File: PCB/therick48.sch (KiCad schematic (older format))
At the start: 125 parts, among them J1 TYPE-C-31-M12_13, J2 AVR-ISP-6, K1 KEYSW, K10 KEYSW, K11 KEYSW, K12 KEYSW, K13 KEYSW, K14 KEYSW, K15 KEYSW, K16 KEYSW, K17 KEYSW, K18 KEYSW, K19 KEYSW, K2 KEYSW, K20 KEYSW, K21 KEYSW, K22 KEYSW, K23 KEYSW, K24 KEYSW, K25 KEYSW, K26 KEYSW, K27 KEYSW, K28 KEYSW, K29 KEYSW, K3 KEYSW, K30 KEYSW, K31 KEYSW, K32 KEYSW, K33 KEYSW, K34 KEYSW, K35 KEYSW, K36 KEYSW, K37 KEYSW, K38 KEYSW, K39 KEYSW, K4 KEYSW, K40 KEYSW, K41 KEYSW, K42 KEYSW, K43 KEYSW, K44 KEYSW, K45 KEYSW, K46 KEYSW, K47 KEYSW, K48 KEYSW, K5 KEYSW, K6 KEYSW, K7 KEYSW, K8 KEYSW, K9 KEYSW, SW1 SW_PUSH, U1 ATMEGA32U4, U2 HOLE, U3 USBLC6-2SC6, U8 HOLE, Y1 16MHz

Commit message: Add Gerbers
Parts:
- removed U8: HOLE, Artwork:QMKBadgeSmall, symbol lets_split-cache:HOLE
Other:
- note removed: "QMK"
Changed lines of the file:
@@
 EESchema Schematic File Version 4
-LIBS:therick-cache
+LIBS:therick48-cache
 EELAYER 29 0
 EELAYER END
@@
 Wire Notes Line
 	9100 4650 9100 6000
-$Comp
-L lets_split-cache:HOLE U8
-U 1 1 5E36C5AD
-P 10100 4250
-F 0 "U8" H 10278 4303 60  0000 L CNN
-F 1 "HOLE" H 10278 4197 60  0000 L CNN
-F 2 "Artwork:QMKBadgeSmall" H 10100 4250 60  0001 C CNN
-F 3 "" H 10100 4250 60  0001 C CNN
-	1    10100 4250
-	1    0    0    -1
-$EndComp
-Text Notes 10000 4300 0    50   ~ 0
-QMK
 NoConn ~ 6700 5200
 NoConn ~ 6700 5300

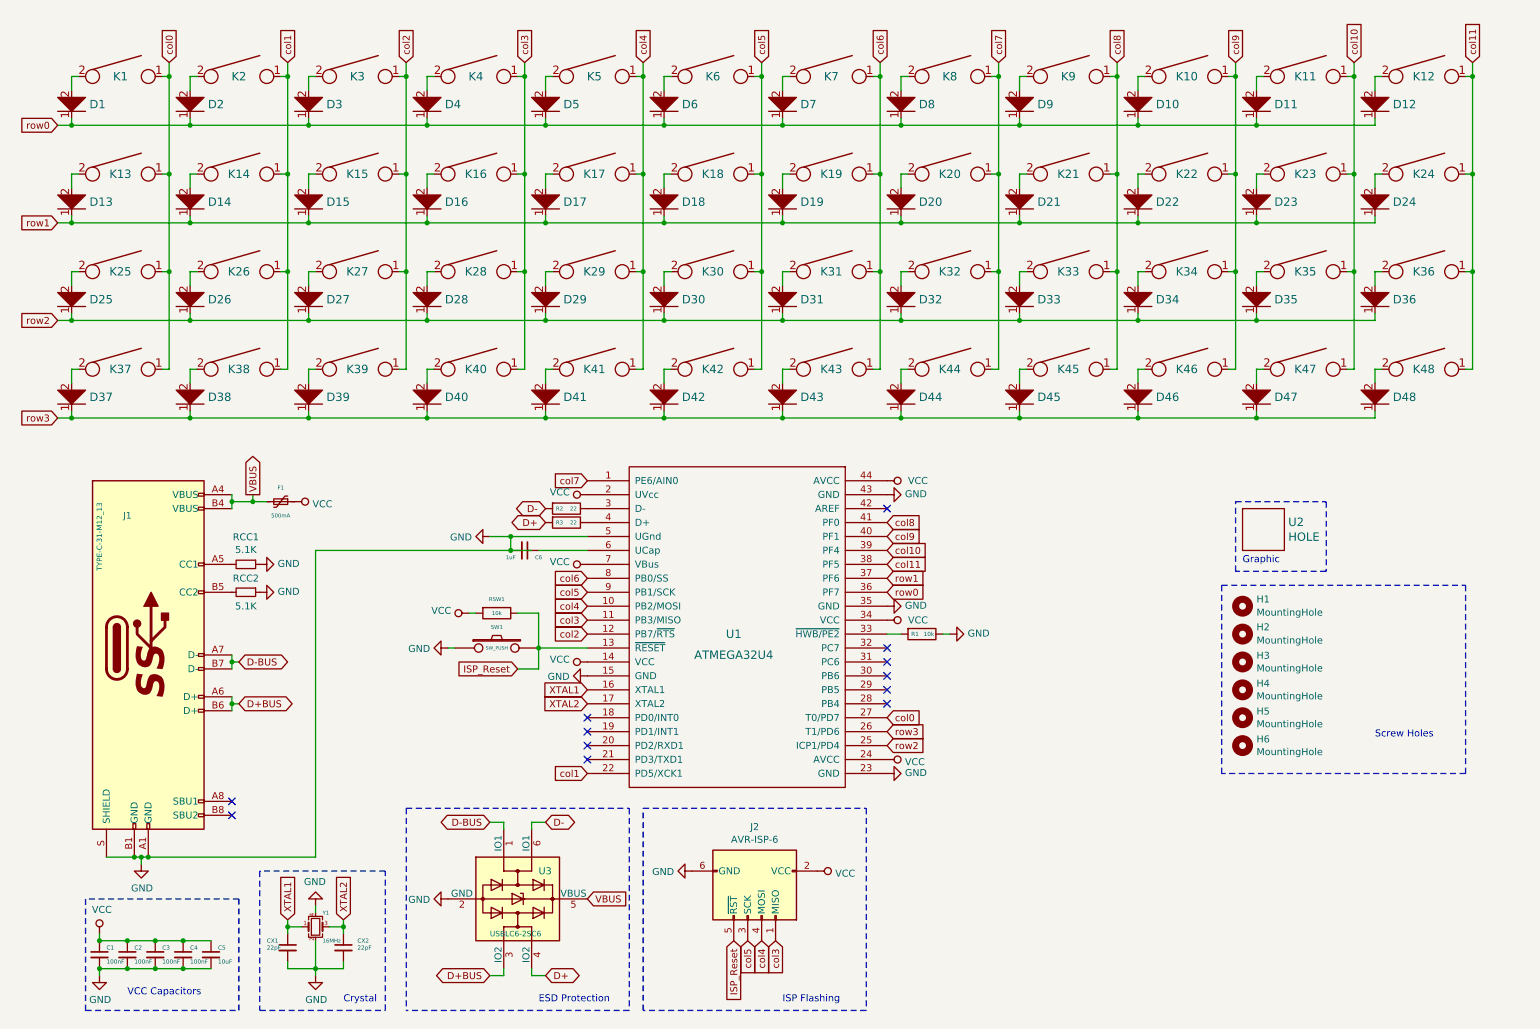
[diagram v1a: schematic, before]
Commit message: Changed pins to make routing cleaner
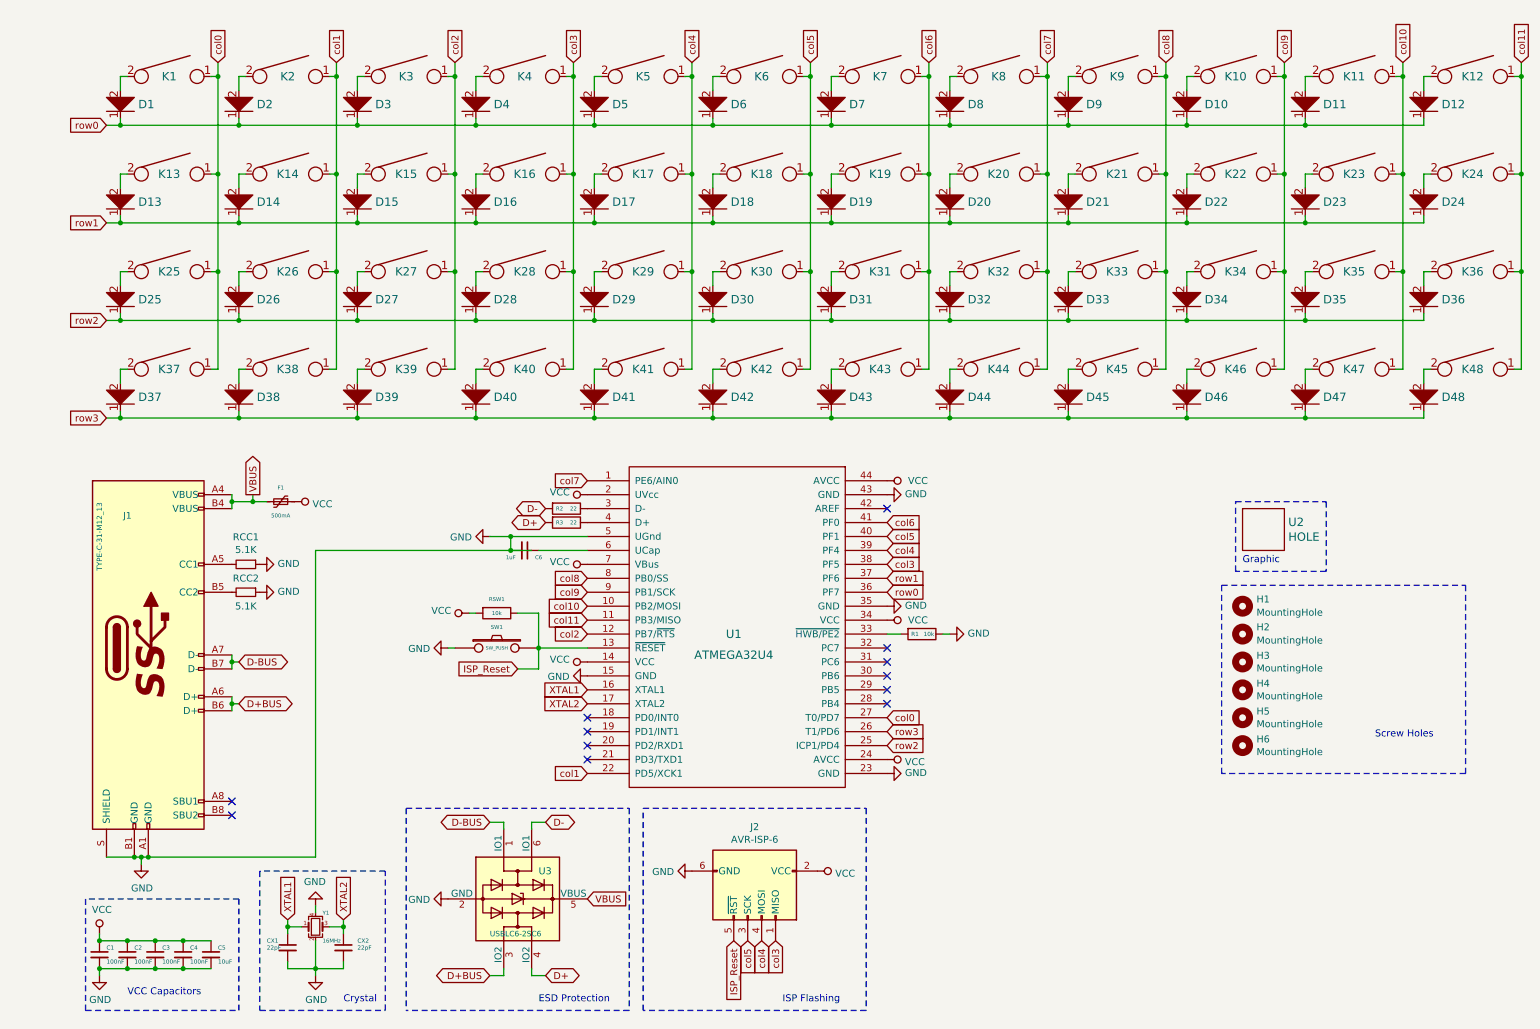
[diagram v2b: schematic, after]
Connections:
- net col10: now also U1.10 (PB2/MOSI); no longer U1.39 (PF4)
- net col11: now also U1.11 (PB3/MISO); no longer U1.38 (PF5)
- net col3: now also U1.38 (PF5); no longer U1.11 (PB3/MISO)
- net col4: now also U1.39 (PF4); no longer U1.10 (PB2/MOSI)
- net col5: now also U1.40 (PF1); no longer U1.9 (PB1/SCK)
- net col6: now also U1.41 (PF0); no longer U1.8 (PB0/SS)
- net col8: now also U1.8 (PB0/SS); no longer U1.41 (PF0)
- net col9: now also U1.9 (PB1/SCK); no longer U1.40 (PF1)
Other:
- moved on the sheet: D1, D10, D11, D12, D13, D14, D15, D16, D17, D18, D19, D2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

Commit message: Updated mounting holes
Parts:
- H1, H2, H3, H4, H5, H6: footprint random-keyboard-parts:Generic-Mounthole -> random-keyboard-parts:plate_hole_4mm_tht
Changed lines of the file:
@@
 F 0 "H1" H 9350 4850 50  0000 L CNN
 F 1 "MountingHole" H 9350 4755 50  0000 L CNN
-F 2 "random-keyboard-parts:Generic-Mounthole" H 9250 4800 50  0001 C CNN
+F 2 "random-keyboard-parts:plate_hole_4mm_tht" H 9250 4800 50  0001 C CNN
 F 3 "~" H 9250 4800 50  0001 C CNN
 	1    9250 4800
@@
 F 0 "H3" H 9350 5246 50  0000 L CNN
 F 1 "MountingHole" H 9350 5155 50  0000 L CNN
-F 2 "random-keyboard-parts:Generic-Mounthole" H 9250 5200 50  0001 C CNN
+F 2 "random-keyboard-parts:plate_hole_4mm_tht" H 9250 5200 50  0001 C CNN
 F 3 "~" H 9250 5200 50  0001 C CNN
 	1    9250 5200
@@
 F 0 "H4" H 9350 5446 50  0000 L CNN
 F 1 "MountingHole" H 9350 5355 50  0000 L CNN
-F 2 "random-keyboard-parts:Generic-Mounthole" H 9250 5400 50  0001 C CNN
+F 2 "random-keyboard-parts:plate_hole_4mm_tht" H 9250 5400 50  0001 C CNN
 F 3 "~" H 9250 5400 50  0001 C CNN
 	1    9250 5400
@@
 F 0 "H5" H 9350 5646 50  0000 L CNN
 F 1 "MountingHole" H 9350 5555 50  0000 L CNN
-F 2 "random-keyboard-parts:Generic-Mounthole" H 9250 5600 50  0001 C CNN
+F 2 "random-keyboard-parts:plate_hole_4mm_tht" H 9250 5600 50  0001 C CNN
 F 3 "~" H 9250 5600 50  0001 C CNN
 	1    9250 5600
@@
 F 0 "H6" H 9350 5846 50  0000 L CNN
 F 1 "MountingHole" H 9350 5755 50  0000 L CNN
-F 2 "random-keyboard-parts:Generic-Mounthole" H 9250 5800 50  0001 C CNN
+F 2 "random-keyboard-parts:plate_hole_4mm_tht" H 9250 5800 50  0001 C CNN
 F 3 "~" H 9250 5800 50  0001 C CNN
 	1    9250 5800
@@
 F 0 "H2" H 9350 5050 50  0000 L CNN
 F 1 "MountingHole" H 9350 4955 50  0000 L CNN
-F 2 "random-keyboard-parts:Generic-Mounthole" H 9250 5000 50  0001 C CNN
+F 2 "random-keyboard-parts:plate_hole_4mm_tht" H 9250 5000 50  0001 C CNN
 F 3 "~" H 9250 5000 50  0001 C CNN
 	1    9250 5000

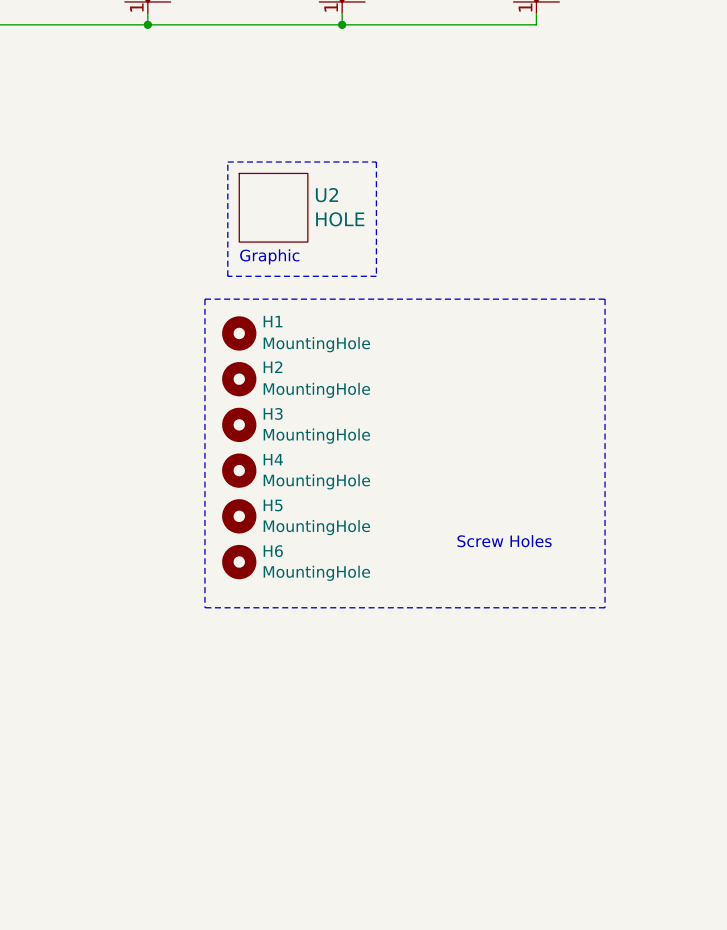
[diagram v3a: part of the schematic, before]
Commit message: Added more mounting holes
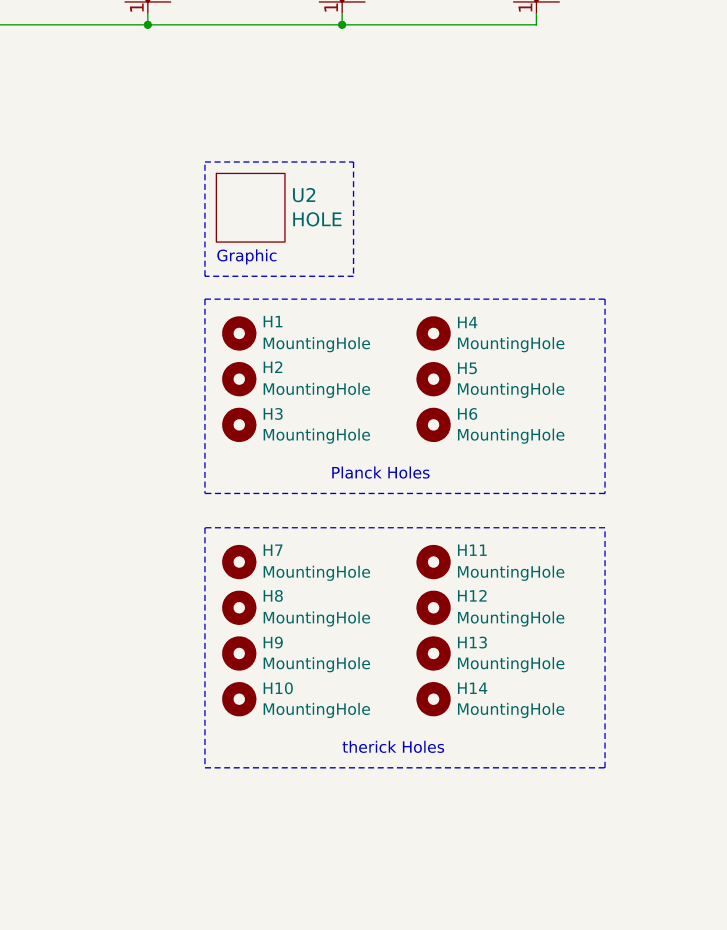
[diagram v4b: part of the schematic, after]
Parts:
- added H10, H11, H12, H13, H14, H7, H8, H9: MountingHole, random-keyboard-parts:plate_hole_4mm_tht, symbol Mechanical:MountingHole
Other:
- note added: "Planck Holes"
- note added: "therick Holes"
- note removed: "Screw Holes"
- moved on the sheet: H4, H5, H6, U2
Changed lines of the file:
@@
 L Mechanical:MountingHole H4
 U 1 1 5DAFCFC0
-P 9250 5400
-F 0 "H4" H 9350 5446 50  0000 L CNN
-F 1 "MountingHole" H 9350 5355 50  0000 L CNN
-F 2 "random-keyboard-parts:plate_hole_4mm_tht" H 9250 5400 50  0001 C CNN
-F 3 "~" H 9250 5400 50  0001 C CNN
-	1    9250 5400
+P 10100 4800
+F 0 "H4" H 10200 4846 50  0000 L CNN
+F 1 "MountingHole" H 10200 4755 50  0000 L CNN
+F 2 "random-keyboard-parts:plate_hole_4mm_tht" H 10100 4800 50  0001 C CNN
+F 3 "~" H 10100 4800 50  0001 C CNN
+	1    10100 4800
 	1    0    0    -1
 $EndComp
@@
 L Mechanical:MountingHole H5
 U 1 1 5DAFD908
-P 9250 5600
-F 0 "H5" H 9350 5646 50  0000 L CNN
-F 1 "MountingHole" H 9350 5555 50  0000 L CNN
-F 2 "random-keyboard-parts:plate_hole_4mm_tht" H 9250 5600 50  0001 C CNN
-F 3 "~" H 9250 5600 50  0001 C CNN
-	1    9250 5600
+P 10100 5000
+F 0 "H5" H 10200 5046 50  0000 L CNN
+F 1 "MountingHole" H 10200 4955 50  0000 L CNN
+F 2 "random-keyboard-parts:plate_hole_4mm_tht" H 10100 5000 50  0001 C CNN
+F 3 "~" H 10100 5000 50  0001 C CNN
+	1    10100 5000
 	1    0    0    -1
 $EndComp
@@
 L Mechanical:MountingHole H6
 U 1 1 5DAFE1B7
-P 9250 5800
-F 0 "H6" H 9350 5846 50  0000 L CNN
-F 1 "MountingHole" H 9350 5755 50  0000 L CNN
-F 2 "random-keyboard-parts:plate_hole_4mm_tht" H 9250 5800 50  0001 C CNN
-F 3 "~" H 9250 5800 50  0001 C CNN
-	1    9250 5800
+P 10100 5200
+F 0 "H6" H 10200 5246 50  0000 L CNN
+F 1 "MountingHole" H 10200 5155 50  0000 L CNN
+F 2 "random-keyboard-parts:plate_hole_4mm_tht" H 10100 5200 50  0001 C CNN
+F 3 "~" H 10100 5200 50  0001 C CNN
+	1    10100 5200
 	1    0    0    -1
 $EndComp
@@
 L lets_split-cache:HOLE U2
 U 1 1 5DE56E92
-P 9400 4250
-F 0 "U2" H 9578 4303 60  0000 L CNN
-F 1 "HOLE" H 9578 4197 60  0000 L CNN
-F 2 "Artwork:rick_large" H 9400 4250 60  0001 C CNN
-F 3 "" H 9400 4250 60  0001 C CNN
-	1    9400 4250
+P 9300 4250
+F 0 "U2" H 9478 4303 60  0000 L CNN
+F 1 "HOLE" H 9478 4197 60  0000 L CNN
+F 2 "Artwork:rick_large" H 9300 4250 60  0001 C CNN
+F 3 "" H 9300 4250 60  0001 C CNN
+	1    9300 4250
 	1    0    0    -1
 $EndComp
@@
 Wire Notes Line
 	2050 6900 950  6900
-Text Notes 10200 5750 0    50   ~ 0
-Screw Holes
-Text Notes 9250 4500 0    50   ~ 0
+Text Notes 9650 5450 0    50   ~ 0
+Planck Holes
+Text Notes 9150 4500 0    50   ~ 0
 Graphic
 Wire Notes Line
-	9200 4550 9200 4050
-Wire Notes Line
-	9200 4050 9850 4050
-Wire Notes Line
-	9850 4050 9850 4550
-Wire Notes Line
-	9850 4550 9200 4550
+	9100 4550 9100 4050
+Wire Notes Line
+	9100 4050 9750 4050
+Wire Notes Line
+	9750 4050 9750 4550
+Wire Notes Line
+	9750 4550 9100 4550
 Text GLabel 2050 5500 2    50   BiDi ~ 0
 D+BUS
@@
 Wire Notes Line
 	9100 4650 10850 4650
-Wire Notes Line
-	10850 4650 10850 6000
-Wire Notes Line
-	10850 6000 9100 6000
-Wire Notes Line
-	9100 4650 9100 6000
 NoConn ~ 6700 5200
 NoConn ~ 6700 5300
@@
 	0    1    1    0
 $EndComp
+$Comp
+L Mechanical:MountingHole H7
+U 1 1 5EB711B5
+P 9250 5800
+F 0 "H7" H 9350 5850 50  0000 L CNN
+F 1 "MountingHole" H 9350 5755 50  0000 L CNN
+F 2 "random-keyboard-parts:plate_hole_4mm_tht" H 9250 5800 50  0001 C CNN
+F 3 "~" H 9250 5800 50  0001 C CNN
+	1    9250 5800
+	1    0    0    -1
+$EndComp
+$Comp
+L Mechanical:MountingHole H9
+U 1 1 5EB711BB
+P 9250 6200
+F 0 "H9" H 9350 6246 50  0000 L CNN
+F 1 "MountingHole" H 9350 6155 50  0000 L CNN
+F 2 "random-keyboard-parts:plate_hole_4mm_tht" H 9250 6200 50  0001 C CNN
+F 3 "~" H 9250 6200 50  0001 C CNN
+	1    9250 6200
+	1    0    0    -1
+$EndComp
+$Comp
+L Mechanical:MountingHole H10
+U 1 1 5EB711C1
+P 9250 6400
+F 0 "H10" H 9350 6446 50  0000 L CNN
+F 1 "MountingHole" H 9350 6355 50  0000 L CNN
+F 2 "random-keyboard-parts:plate_hole_4mm_tht" H 9250 6400 50  0001 C CNN
+F 3 "~" H 9250 6400 50  0001 C CNN
+	1    9250 6400
+	1    0    0    -1
+$EndComp
+$Comp
+L Mechanical:MountingHole H8
+U 1 1 5EB711C7
+P 9250 6000
+F 0 "H8" H 9350 6050 50  0000 L CNN
+F 1 "MountingHole" H 9350 5955 50  0000 L CNN
+F 2 "random-keyboard-parts:plate_hole_4mm_tht" H 9250 6000 50  0001 C CNN
+F 3 "~" H 9250 6000 50  0001 C CNN
+	1    9250 6000
+	1    0    0    -1
+$EndComp
+$Comp
+L Mechanical:MountingHole H11
+U 1 1 5EB954D0
+P 10100 5800
+F 0 "H11" H 10200 5850 50  0000 L CNN
+F 1 "MountingHole" H 10200 5755 50  0000 L CNN
+F 2 "random-keyboard-parts:plate_hole_4mm_tht" H 10100 5800 50  0001 C CNN
+F 3 "~" H 10100 5800 50  0001 C CNN
+	1    10100 5800
+	1    0    0    -1
+$EndComp
+$Comp
+L Mechanical:MountingHole H13
+U 1 1 5EB954D6
+P 10100 6200
+F 0 "H13" H 10200 6246 50  0000 L CNN
+F 1 "MountingHole" H 10200 6155 50  0000 L CNN
+F 2 "random-keyboard-parts:plate_hole_4mm_tht" H 10100 6200 50  0001 C CNN
+F 3 "~" H 10100 6200 50  0001 C CNN
+	1    10100 6200
+	1    0    0    -1
+$EndComp
+$Comp
+L Mechanical:MountingHole H14
+U 1 1 5EB954DC
+P 10100 6400
+F 0 "H14" H 10200 6446 50  0000 L CNN
+F 1 "MountingHole" H 10200 6355 50  0000 L CNN
+F 2 "random-keyboard-parts:plate_hole_4mm_tht" H 10100 6400 50  0001 C CNN
+F 3 "~" H 10100 6400 50  0001 C CNN
+	1    10100 6400
+	1    0    0    -1
+$EndComp
+$Comp
+L Mechanical:MountingHole H12
+U 1 1 5EB954E2
+P 10100 6000
+F 0 "H12" H 10200 6050 50  0000 L CNN
+F 1 "MountingHole" H 10200 5955 50  0000 L CNN
+F 2 "random-keyboard-parts:plate_hole_4mm_tht" H 10100 6000 50  0001 C CNN
+F 3 "~" H 10100 6000 50  0001 C CNN
+	1    10100 6000
+	1    0    0    -1
+$EndComp
+Wire Notes Line
+	10850 5500 9100 5500
+Wire Notes Line
+	10850 4650 10850 5500
+Wire Notes Line
+	9100 4650 9100 5500
+Wire Notes Line
+	9100 5650 9100 6700
+Wire Notes Line
+	9100 6700 10850 6700
+Wire Notes Line
+	10850 6700 10850 5650
+Wire Notes Line
+	10850 5650 9100 5650
+Text Notes 9700 6650 0    50   ~ 0
+therick Holes
 $EndSCHEMATC

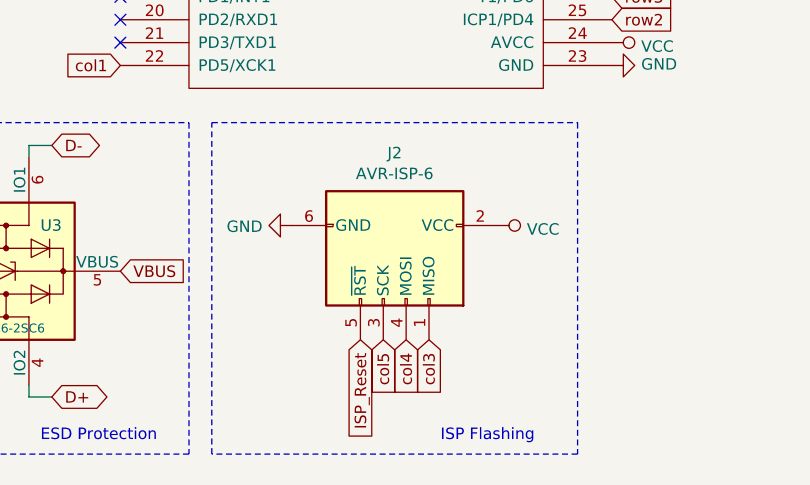
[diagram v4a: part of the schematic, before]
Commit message: Made ISP header actually work
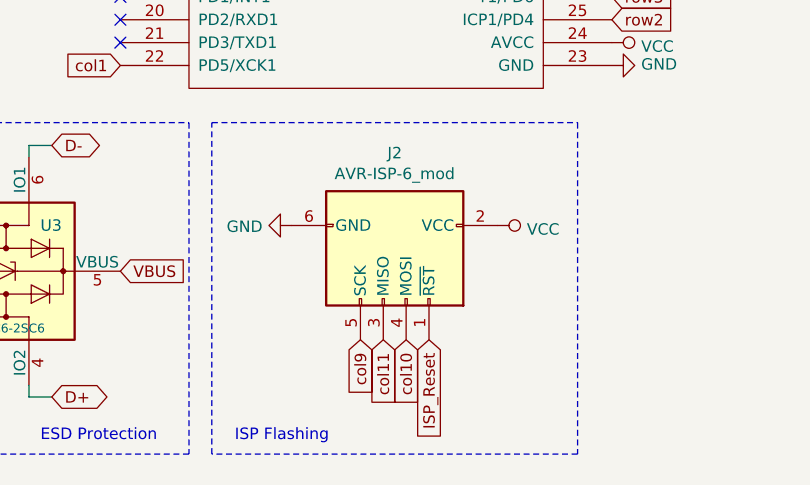
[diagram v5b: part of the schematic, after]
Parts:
- removed J2: AVR-ISP-6, Keeb_footprints:PIN_HEADER_1x6_OFFSET, symbol Connector:AVR-ISP-6
- added J2: AVR-ISP-6_mod, Keeb_footprints:PIN_HEADER_1x6_OFFSET, symbol Connector:AVR-ISP-6_mod
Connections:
- net GND: now also J2.6 (GND)
- net ISP_Reset: now also J2.1 (~RST)
- net VCC: now also J2.2 (VCC)
- net col10: now also J2.4 (MOSI)
- net col11: now also J2.3 (MISO)
- net col9: now also J2.5 (SCK)
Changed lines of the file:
@@
-	0    1    1    0
-$EndComp
-$Comp
-L Connector:AVR-ISP-6 J2
-U 1 1 5E280E11
-P 5700 6800
-F 0 "J2" V 5283 6850 50  0000 C CNN
-F 1 "AVR-ISP-6" V 5374 6850 50  0000 C CNN
-F 2 "Keeb_footprints:PIN_HEADER_1x6_OFFSET" V 5450 6850 50  0001 C CNN
-F 3 " ~" H 4425 6250 50  0001 C CNN
-	1    5700 6800
 	0    1    1    0
 $EndComp
 Text GLabel 5800 7200 3    50   Input ~ 0
-col4
-Text GLabel 5900 7200 3    50   Input ~ 0
-col3
+col10
 Text GLabel 5700 7200 3    50   Input ~ 0
-col5
+col11
+Text GLabel 5600 7200 3    50   Input ~ 0
+col9
 $Comp
 L power:GND #PWR0121
@@
 Text GLabel 4050 5250 0    50   Input ~ 0
 ISP_Reset
-Text GLabel 5600 7200 3    50   Input ~ 0
+Text GLabel 5900 7200 3    50   Input ~ 0
 ISP_Reset
-Text Notes 5950 7650 0    50   ~ 0
+Text Notes 5050 7650 0    50   ~ 0
 ISP Flashing
 Wire Notes Line
@@
 Text Notes 9700 6650 0    50   ~ 0
 therick Holes
+$Comp
+L Connector:AVR-ISP-6_mod J2
+U 1 1 5EC003A1
+P 5700 6800
+F 0 "J2" V 5283 6850 50  0000 C CNN
+F 1 "AVR-ISP-6_mod" V 5374 6850 50  0000 C CNN
+F 2 "Keeb_footprints:PIN_HEADER_1x6_OFFSET" V 5450 6850 50  0001 C CNN
+F 3 " ~" H 4425 6250 50  0001 C CNN
+	1    5700 6800
+	0    1    1    0
+$EndComp
 $EndSCHEMATC
